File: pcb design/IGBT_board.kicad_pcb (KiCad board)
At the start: 4 copper layers, 162 x 100 mm, 257 parts, among them J1 CONN-100MIL-M-2x8, J2 DESAT, J3 DESAT, J4 PHASE, J5 PHASE CURRENT CONN, Q1 IGBT, Q10 IGBT, Q11 IGBT, Q12 IGBT, Q13 NPN, Q14 PNP, Q15 CSD19533Q5A, Q16 CSD19533Q5A, Q17 NPN, Q18 PNP, Q19 PNP, Q2 IGBT, Q20 PNP, Q3 IGBT, Q4 IGBT, Q5 IGBT, Q6 IGBT, Q7 IGBT, Q8 IGBT, Q9 IGBT, T1 TRANS-3-1CT, U1 ISO5852S, U10 AMC1301, U11 SI8710B, U12 OPA2172, U13 LM3480, U14 LM3480, U2 LM5030, U3 ISO5852S, U5 LM1117IMP-v.v, U8 SI8710B, U9 OPA2172

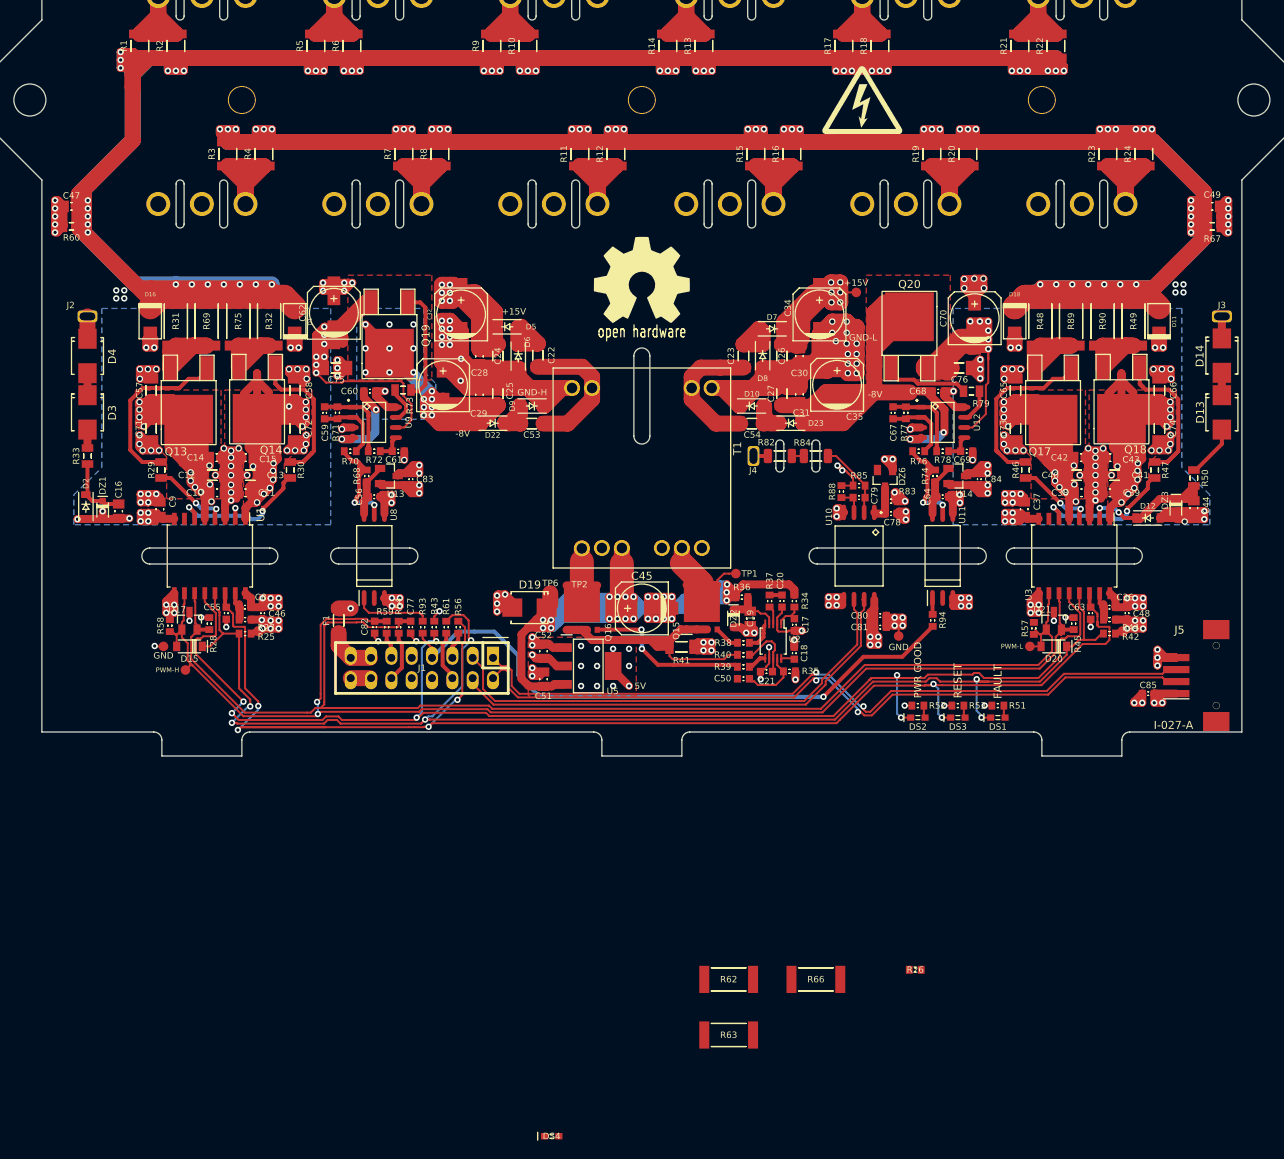
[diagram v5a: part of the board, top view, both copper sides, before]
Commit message: Add gate driver load to enable 2 step turnoff in buffered configuration. Updated layout.
Signed-off-by: Marcos Chaparro <mchaparro@paltatech.com>
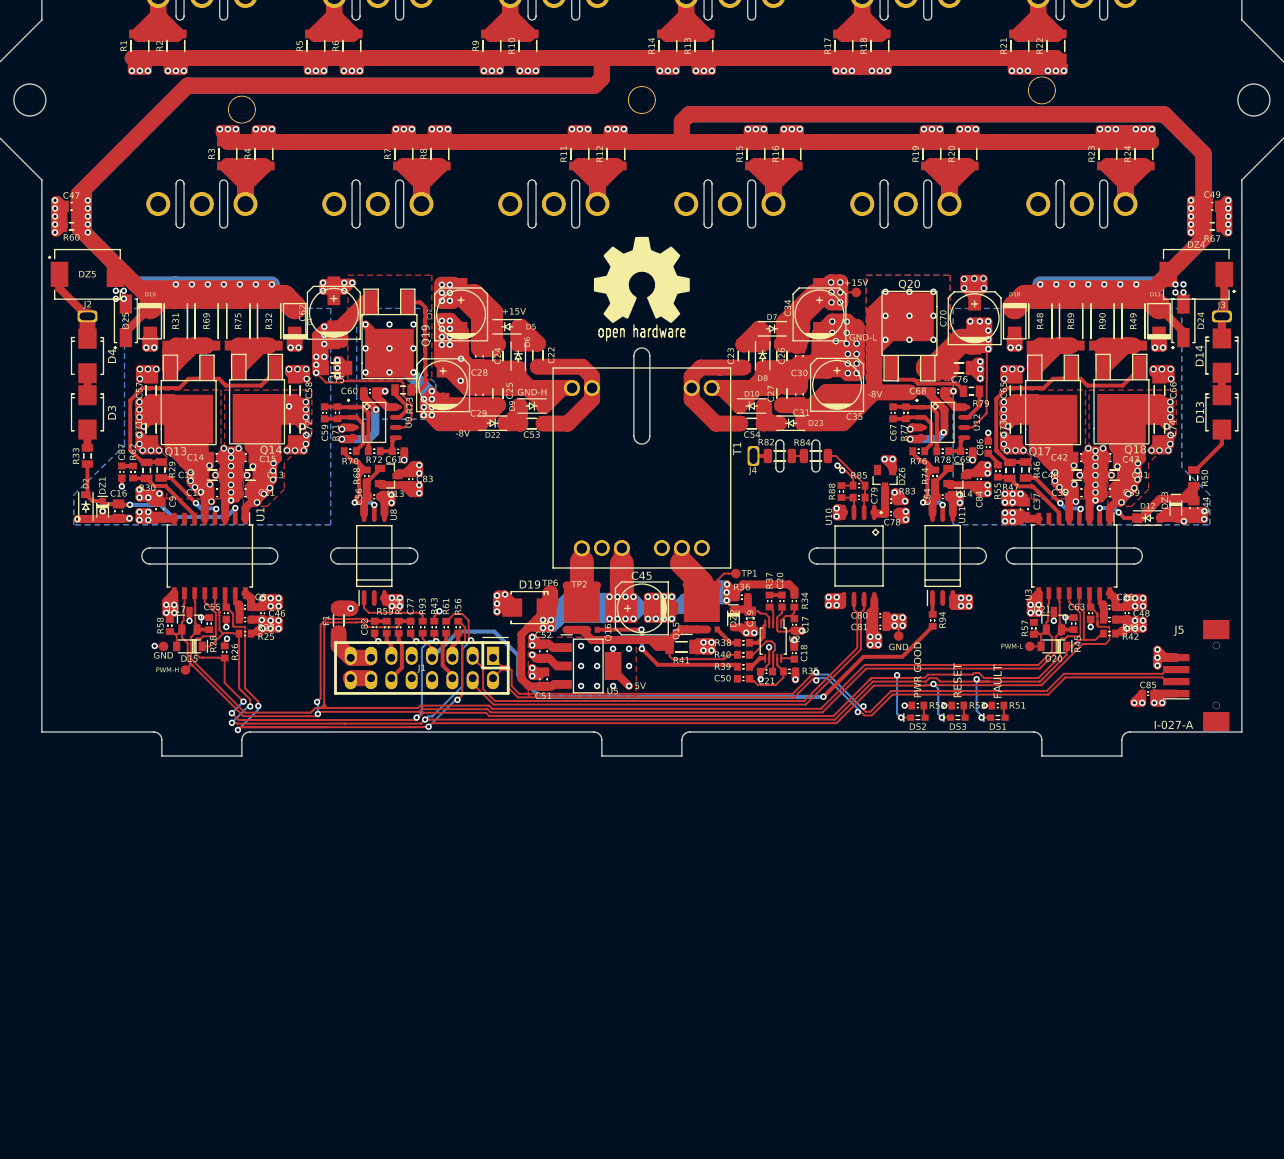
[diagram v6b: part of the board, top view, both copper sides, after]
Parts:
- removed DS4: CAPS_CHARGED, smd-semi:LED-0603
- removed G***: LOGO, w_logo:Logo_silk_high_voltage_10x8.5mm
- removed R63, R66: 50k 1W, IPC7351-Nominal:RESC6432X70
- added C86: 10nF, IPC7351-Nominal:CAPC1608X55, F.Cu at (43.3, 11.4)
- added C87: 10nF, IPC7351-Nominal:CAPC1608X55, F.Cu at (-65.0, 14.5)
- added D24: ES2J-LTP, IPC7351-Nominal:DIOM5226X203, F.Cu at (67.7, -4.40)
- added D25: ES2J-LTP, IPC7351-Nominal:DIOM5226X203, F.Cu at (-64.5, -4.40)
- added DZ4: SMCJ440CA, IPC7351-Nominal:DIOM7959X265, F.Cu at (69.3, -10.2)
- added DZ5: SMCJ440CA, IPC7351-Nominal:DIOM7959X265, F.Cu at (-69.3, -10.2)
- added R55: 12R, IPC7351-Nominal:RESC1608X50, F.Cu at (44.5, 14.4)
- D12, D2: value RB160MM-60TR -> RB168MM-60TR
- DZ2: value 12v zener -> MM3Z12VB
- R1, R2: value 20R -> 1R
- R29, R30, R46, R47: value 0R5 -> 12R
- R62: value 50k 1W -> 12R; footprint IPC7351-Nominal:RESC6432X70 -> IPC7351-Nominal:RESC1608X50
- moved R62 97.8 mm to (-63.6, 14.5), turned to 270 degrees
- moved R26 95.0 mm to (-52.1, 37.0), turned to 270 degrees
- moved R47 18.1 mm to (46.0, 14.3)
- moved R30 18.0 mm to (-61.9, 14.3)
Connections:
- Q14 pad 1: Net-(Q14-Pad1) -> Net-(Q13-Pad1)
- Q18 pad 1: Net-(Q18-Pad1) -> Net-(Q17-Pad1)
- R30 pad 1: Net-(Q14-Pad1) -> Net-(Q13-Pad1)
- R47 pad 1: Net-(Q18-Pad1) -> Net-(Q17-Pad1)
- R62 pad 2: VBUS+ -> Net-(R30-Pad2)
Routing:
- net VBUS-: track 704.6 -> 821.5 mm, vias 80 -> 81
- net GATE_LOW: track 595.5 -> 703.6 mm
- net GATE_HIGH: track 618.4 -> 722.7 mm
- net PHASE: track 694.3 -> 794.6 mm, vias 70 -> 69
- net Net-(Q18-Pad1): track 19.7 -> 0.00 mm
- net Net-(Q14-Pad1): track 19.7 -> 0.00 mm
- net Net-(C16-Pad1): track 10.0 -> 25.7 mm, vias 1 -> 2
- net Net-(Q13-Pad1): track 22.1 -> 33.9 mm
- net Net-(Q17-Pad1): track 22.3 -> 33.9 mm
- net /IGBT_driver_TOP/-VEE: track 138.9 -> 127.4 mm, vias 25 -> 26
- net /IGBT_driver_BOT/-VEE: track 117.2 -> 106.1 mm, vias 23 -> 24
- net Net-(R30-Pad2): track 17.9 -> 10.1 mm, vias 2 -> 0
- net Net-(R47-Pad2): track 17.9 -> 10.2 mm, vias 2 -> 0
- net VBUS+: track 2.80 -> 9.50 mm
- net Net-(C86-Pad1): track 0.00 -> 2.00 mm
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- added copper zone on B.Cu, net /IGBT_driver_BOT/-15V
